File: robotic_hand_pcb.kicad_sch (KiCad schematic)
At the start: 41 parts, among them J1 TC2050-IDC, J2 2171750001, SW1 SPST, SW2 SPST, U1 ld39150dt33-r, U2 STM32F446RET, U3 TXB0104QPWRQ1, Y1 8M, Y2 32k768

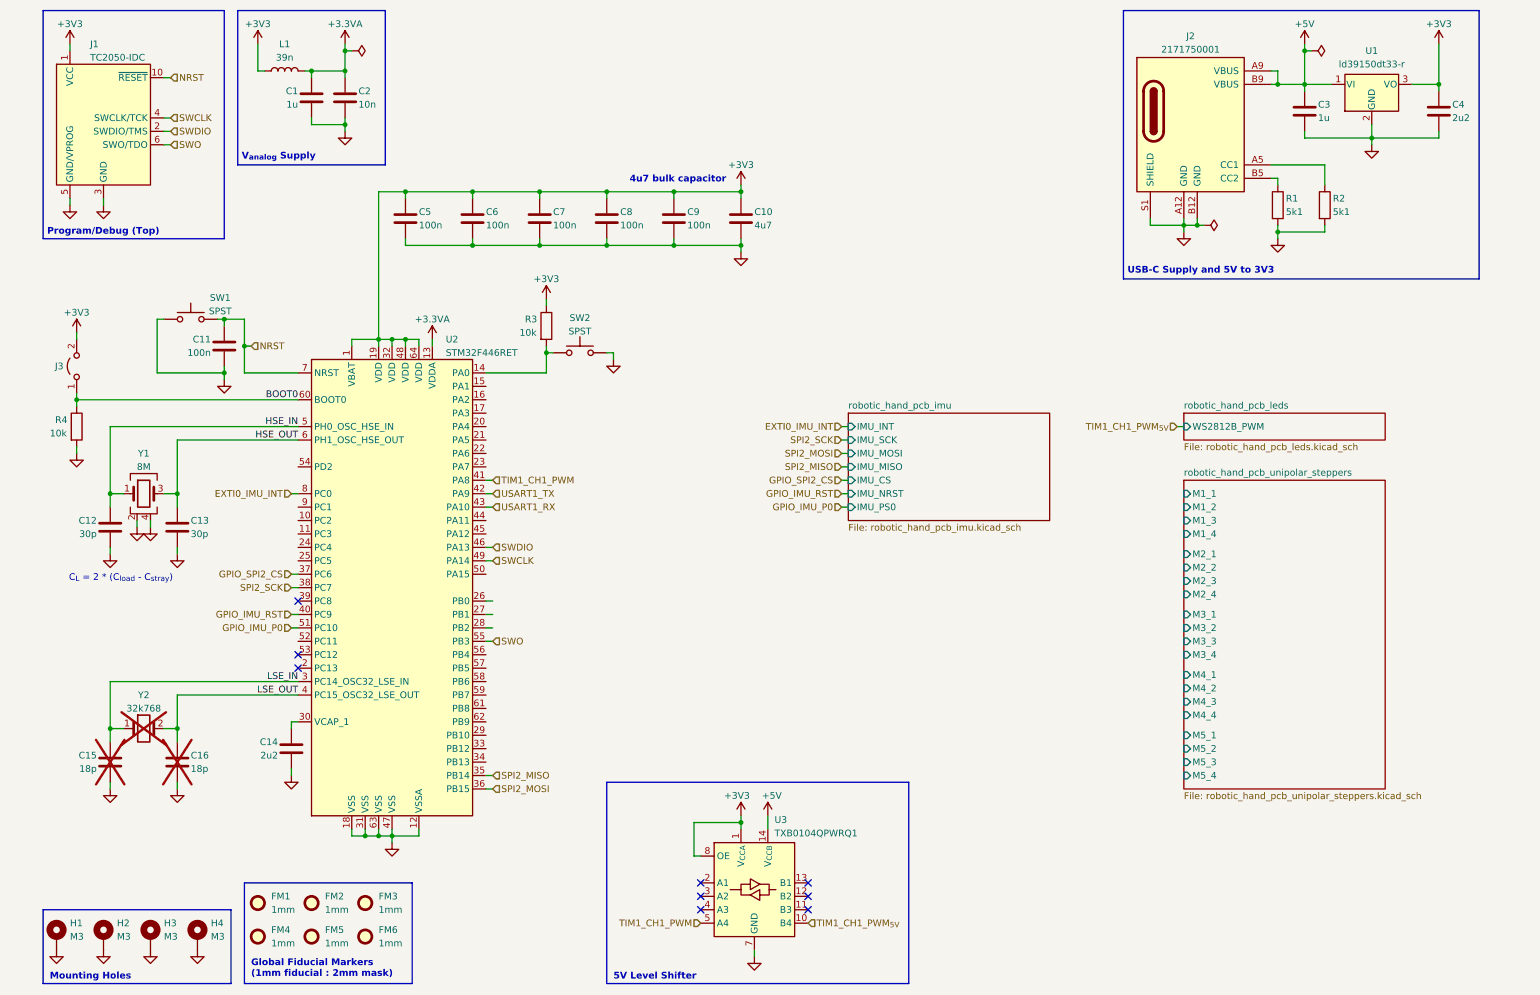
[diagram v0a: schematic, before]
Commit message: Add 5V buck regulator
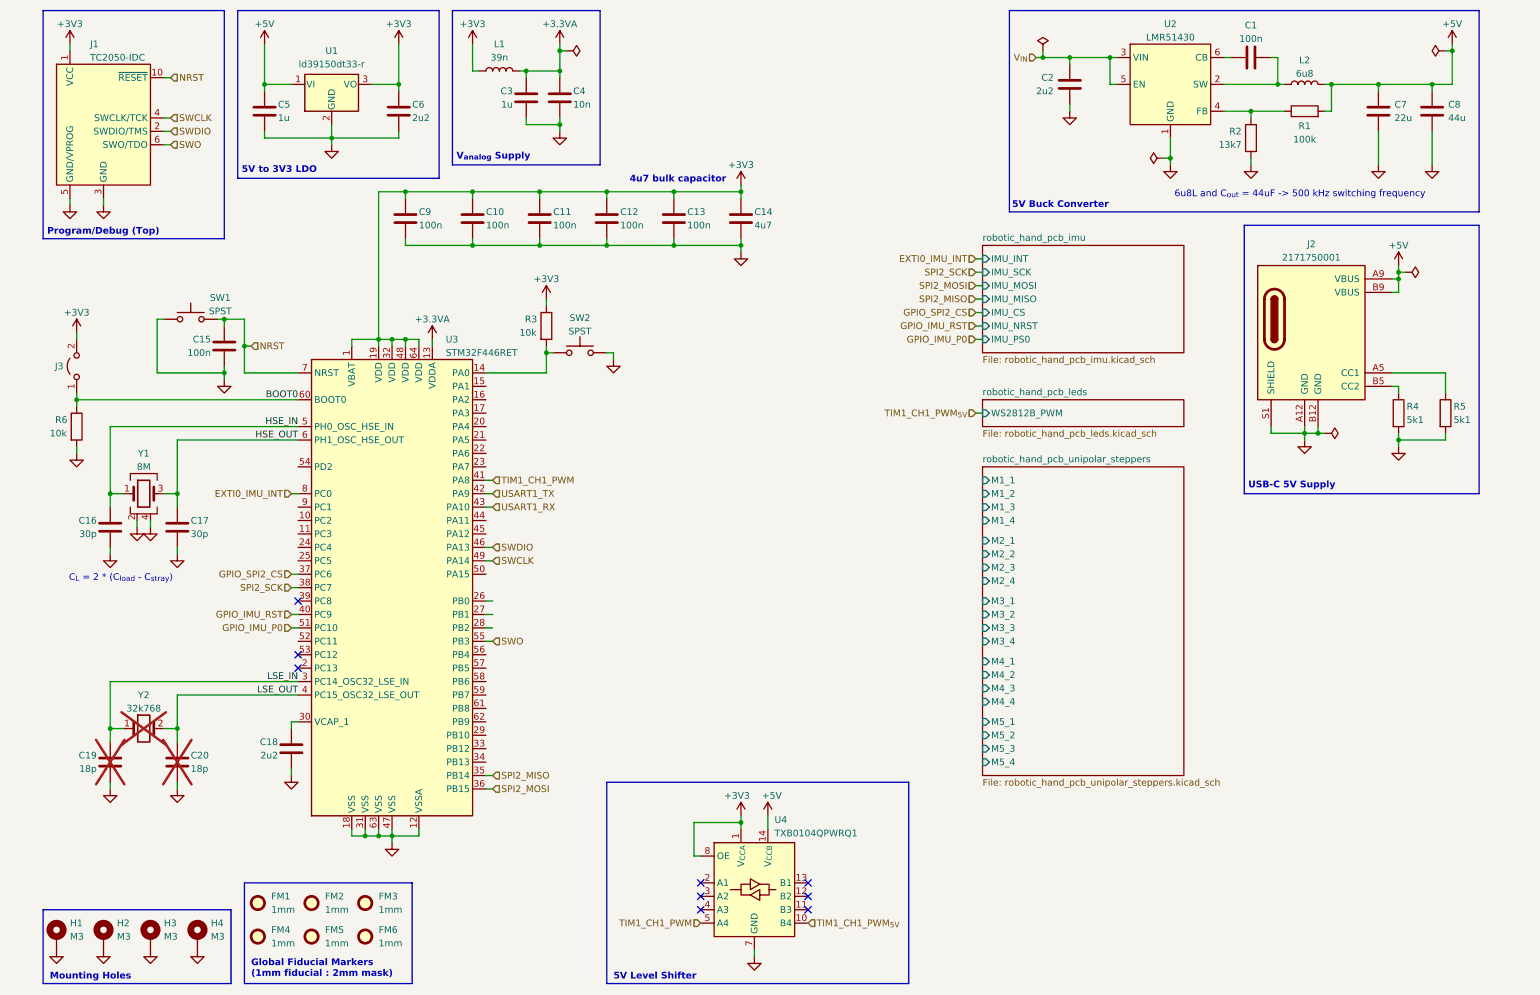
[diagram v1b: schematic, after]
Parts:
- added C1: 100n, symbol Device:C
- added C2: 2u2, symbol Device:C
- added C7: 22u, symbol Device:C
- added C8: 44u, symbol Device:C
- added L2: 6u8, symbol Device:L
- added R1: 100k, symbol Device:R
- added R2: 13k7, symbol Device:R
- added U2: LMR51430, ti_buck:lmr51430, symbol ti_buck:lmr51430
- renumbered C6 to C10, C7 to C11, C8 to C12, C9 to C13, C10 to C14, C11 to C15, C12 to C16, C13 to C17, C14 to C18, C15 to C19, C16 to C20, C1 to C3, C2 to C4, C3 to C5, C4 to C6, C5 to C9, R1 to R4, R2 to R5, R4 to R6, U2 to U3, U3 to U4
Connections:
- net +5V: now also C7.2, C8.2, L2.2, R1.2
- net GND: now also C2.2, C7.1, C8.1, R2.2, U2.1 (GND)
- new net: C1.2, L2.1, U2.2 (SW)
- new net: R1.1, R2.1, U2.4 (FB)
- new net: C1.1, U2.6 (CB)
- new net V_{IN}: C2.1, U2.3 (VIN), U2.5 (EN)
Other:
- note added: "5V Buck Converter"
- note added: "5V to 3V3 LDO"
- note added: "6u8L and C_{out} = 44uF -> 500 kHz switching frequency"
- note added: "USB-C 5V Supply"
- note removed: "USB-C Supply and 5V to 3V3"
- moved on the sheet: C3, C4, C5, C6, J2, L1, R4, R5, U1

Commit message: Pass ERC
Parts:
- removed R3: 10k, Resistor_SMD:R_0603_1608Metric, symbol Device:R
- removed SW2: SPST, Button_Switch_THT:SW_PUSH_6mm, symbol Switch:SW_Push
- added J16: UART, symbol Connector:Conn_01x02_Pin
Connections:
- net USART1_RX: now also J16.2 (Pin_2)
- net USART1_TX: now also J16.1 (Pin_1)
- net ADC_IN12: now reaches U3.10 (PC2)
- net ADC_IN13: now reaches U3.11 (PC3)
- net TIM2_CH1_PWM: now reaches U3.14 (PA0)
- net TIM2_CH2_PWM: now reaches U3.15 (PA1)
- net TIM2_CH3_PWM: now reaches U3.16 (PA2)
- net ADC_IN3: now reaches U3.17 (PA3)
- net ADC_IN4: now reaches U3.20 (PA4)
- net ADC_IN5: now reaches U3.21 (PA5)
- net TIM3_CH1_PWM: now reaches U3.22 (PA6)
- net TIM3_CH2_PWM: now reaches U3.23 (PA7)
- net ADC_IN14: now reaches U3.24 (PC4)
- net ADC_IN15: now reaches U3.25 (PC5)
- net TIM3_CH3_PWM: now reaches U3.26 (PB0)
- net TIM3_CH4_PWM: now reaches U3.27 (PB1)
- net TIM2_CH4_PWM: now reaches U3.28 (PB2)
- net EXTI8_IMU_INT: now reaches U3.39 (PC8)
- net EXTI5_TOF_INT: now reaches U3.57 (PB5)
- net I2C1_SCL: now reaches U3.58 (PB6)
- net I2C1_SDA: now reaches U3.59 (PB7)
- net ADC_IN11: now reaches U3.9 (PC1)
- net EXTI0_IMU_INT renamed ADC_IN10
- no-connect marks 9 -> 19
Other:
- sheet robotic_hand_pcb_unipolar_steppers renamed robotic_hand_pcb_servos
- added sheet robotic_hand_pcb_tof (robotic_hand_pcb_tof.kicad_sch)
- sheet robotic_hand_pcb_leds ports: added ADC_PHOTODIODE; removed none
- sheet robotic_hand_pcb_servos: file robotic_hand_pcb_unipolar_steppers.kicad_sch -> robotic_hand_pcb_servos.kicad_sch
- sheet robotic_hand_pcb_servos ports: added SERVO_1_ISENSE, SERVO_1_PWM, SERVO_2_ISENSE, SERVO_2_PWM, SERVO_3_ISENSE, SERVO_3_PWM, SERVO_4_ISENSE, SERVO_4_PWM, SERVO_5_ISENSE, SERVO_5_PWM, SERVO_6_ISENSE, SERVO_6_PWM, SERVO_7_ISENSE, SERVO_7_PWM, SERVO_8_ISENSE, SERVO_8_PWM; removed M1_1, M1_2, M1_3, M1_4, M2_1, M2_2, M2_3, M2_4, M3_1, M3_2, M3_3, M3_4, M4_1, M4_2, M4_3, M4_4, M5_1, M5_2, M5_3, M5_4
- note added: "UART Breakout"

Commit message: Update for WIP changes
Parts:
- removed C3: 1u, Capacitor_SMD:C_0603_1608Metric, symbol Device:C
- removed C4: 10n, Capacitor_SMD:C_0603_1608Metric, symbol Device:C
- removed L1: 39n, Inductor_SMD:L_0402_1005Metric, symbol Device:L
- removed U1: ld39150dt33-r, common:to-252-2_dpak-2-leg, symbol common:ld39150dt33-r
- added C12: 100n, Capacitor_SMD:C_0603_1608Metric, symbol Device:C
- added U2: ld39150dt33-r, common:to-252-2_dpak-2-leg, symbol common:ld39150dt33-r
- renumbered C12 to C10, C13 to C11, C14 to C13, C15 to C14, C16 to C15, C17 to C16, C18 to C17, C19 to C18, C20 to C19, C7 to C3, C8 to C4, C9 to C7, C10 to C8, C11 to C9, J2 to J1, J1 to J2, J16 to J4, L2 to L1, R4 to R3, R5 to R4, R6 to R5, U2 to U1, U4 to U3, U3 to U4
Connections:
- net +3.3VA is gone; now on net +3V3: U4.13 (VDDA)
- net ADC_IN14 is gone; now on net GPIO_IMU_RST: U4.24 (PC4)
- net ADC_IN15 is gone; now on net GPIO_IMU_P0: U4.25 (PC5)
- net +3V3: now also C12.1, U2.3 (VO)
- net +5V: now also U2.1 (VI)
- net GND: now also C12.2, U2.2 (GND)
- net GPIO_IMU_P0: no longer U4.51 (PC10)
- net GPIO_IMU_RST: no longer U4.40 (PC9)
- net GPIO_ADC_SYNC: now reaches U4.44 (PA11)
- net GPIO_ADC_RST: now reaches U4.45 (PA12)
- net GPIO_SPI3_CS: now reaches U4.50 (PA15)
- net SPI3_MISO: now reaches U4.52 (PC11)
- net SPI3_MOSI: now reaches U4.53 (PC12)
- net EXTI2_ADC_DRDY: now reaches U4.54 (PD2)
- net EXTI4_TOF_INT: now reaches U4.56 (PB4)
- net ADC_IN10: no longer names the net of U4.8 (PC0)
- net ADC_IN11: no longer names the net of U4.9 (PC1)
- net ADC_IN12: no longer names the net of U4.10 (PC2)
- net ADC_IN13: no longer names the net of U4.11 (PC3)
- net ADC_IN3 renamed EXTI3_IMU_INT
- net ADC_IN4 renamed GPIO_SPI1_CS
- net ADC_IN5 renamed SPI1_SCK
- net EXTI5_TOF_INT renamed GPIO_TOF_XSHUT
- net EXTI8_IMU_INT: no longer names the net of U4.39 (PC8)
- net GPIO_SPI2_CS: no longer names the net of U4.37 (PC6)
- net SPI2_MISO: no longer names the net of U4.35 (PB14)
- net SPI2_MOSI: no longer names the net of U4.36 (PB15)
- net SPI2_SCK: no longer names the net of U4.38 (PC7)
- net TIM2_CH1_PWM: no longer names the net of U4.14 (PA0)
- net TIM2_CH2_PWM: no longer names the net of U4.15 (PA1)
- net TIM2_CH3_PWM: no longer names the net of U4.16 (PA2)
- net TIM2_CH4_PWM: no longer names the net of U4.28 (PB2)
- net TIM3_CH1_PWM renamed SPI1_MISO
- net TIM3_CH2_PWM renamed SPI1_MOSI
- net TIM3_CH3_PWM: no longer names the net of U4.26 (PB0)
- net TIM3_CH4_PWM: no longer names the net of U4.27 (PB1)
- new net SPI3_SCK: U4.51 (PC10)
- no-connect marks 19 -> 6
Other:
- sheet robotic_hand_pcb_servos renamed robotic_hand_pcb_unipolar_steppers
- added sheet robotic_hand_pcb_analog (robotic_hand_pcb_analog.kicad_sch)
- sheet robotic_hand_pcb_leds ports: added none; removed ADC_PHOTODIODE
- sheet robotic_hand_pcb_tof ports: added TOF_XSHUT; removed none
- sheet robotic_hand_pcb_unipolar_steppers: file robotic_hand_pcb_servos.kicad_sch -> robotic_hand_pcb_unipolar_steppers.kicad_sch
- sheet robotic_hand_pcb_unipolar_steppers ports: added M1_1, M1_2, M1_3, M1_4, M2_1, M2_2, M2_3, M2_4, M3_1, M3_2, M3_3, M3_4, M4_1, M4_2, M4_3, M4_4, M5_1, M5_2, M5_3, M5_4; removed SERVO_1_ISENSE, SERVO_1_PWM, SERVO_2_ISENSE, SERVO_2_PWM, SERVO_3_ISENSE, SERVO_3_PWM, SERVO_4_ISENSE, SERVO_4_PWM, SERVO_5_ISENSE, SERVO_5_PWM, SERVO_6_ISENSE, SERVO_6_PWM, SERVO_7_ISENSE, SERVO_7_PWM, SERVO_8_ISENSE, SERVO_8_PWM
- note removed: "V_{analog} Supply"
- moved on the sheet: C1, C10, C11, C13, C2, C3, C4, C7, C8, C9, J1, L1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

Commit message: Add WIP schematic changes
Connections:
- net M1_1: now also U4.8 (PC0)
- net M1_2: now also U4.9 (PC1)
- net M1_3: now also U4.10 (PC2)
- net M1_4: now also U4.11 (PC3)
- net M2_1: now also U4.37 (PC6)
- net M2_2: now also U4.38 (PC7)
- net M2_3: now also U4.39 (PC8)
- net M2_4: now also U4.40 (PC9)
- net M3_1: now also U4.14 (PA0)
- net M3_2: now also U4.15 (PA1)
- net M3_3: now also U4.16 (PA2)
- net M3_4: now also U4.26 (PB0)
- net M4_1: now also U4.27 (PB1)
- net M4_2: now also U4.28 (PB2)
- net M4_3: now also U4.61 (PB8)
- net M4_4: now also U4.62 (PB9)
- net M5_1: now also U4.33 (PB12)
- net M5_2: now also U4.34 (PB13)
- net M5_3: now also U4.35 (PB14)
- net M5_4: now also U4.36 (PB15)
- no-connect marks 6 -> 8
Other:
- sheet robotic_hand_pcb_analog ports: added ADC_CS, ADC_DRDY, ADC_MISO, ADC_MOSI, ADC_RST, ADC_SCK, ADC_SYNC; removed none
- sheet robotic_hand_pcb_tof ports: added TOF_SCL, TOF_SDA; removed I2C_SCL, I2C_SDA
- moved on the sheet: J4

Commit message: Assign footprints
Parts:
- C1, C2, C3, C4: footprint (none) -> Capacitor_SMD:C_0603_1608Metric
- J4: footprint (none) -> Connector_PinHeader_2.54mm:PinHeader_1x02_P2.54mm_Vertical
- L1, R1, R2: footprint (none) -> Resistor_SMD:R_0603_1608Metric
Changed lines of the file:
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@@
 			)
 		)
-		(property "Footprint" ""
+		(property "Footprint" "Resistor_SMD:R_0603_1608Metric"
 			(at 105.41 26.67 0)
 			(effects
@@
 			)
 		)
-		(property "Footprint" ""
+		(property "Footprint" "Resistor_SMD:R_0603_1608Metric"
 			(at 97.028 36.83 90)
 			(effects
@@
 			)
 		)
-		(property "Footprint" ""
+		(property "Footprint" "Capacitor_SMD:C_0603_1608Metric"
 			(at 118.4148 27.94 0)
 			(effects
@@
 			)
 		)
-		(property "Footprint" ""
+		(property "Footprint" "Connector_PinHeader_2.54mm:PinHeader_1x02_P2.54mm_Vertical"
 			(at 105.41 187.96 0)
 			(effects
@@
 			)
 		)
-		(property "Footprint" ""
+		(property "Footprint" "Capacitor_SMD:C_0603_1608Metric"
 			(at 128.5748 27.94 0)
 			(effects
@@
 			)
 		)
-		(property "Footprint" ""
+		(property "Footprint" "Capacitor_SMD:C_0603_1608Metric"
 			(at 99.06 20.6248 0)
 			(effects
@@
 			)
 		)
-		(property "Footprint" ""
+		(property "Footprint" "Resistor_SMD:R_0603_1608Metric"
 			(at 105.41 33.528 90)
 			(effects
@@
 			)
 		)
-		(property "Footprint" ""
+		(property "Footprint" "Capacitor_SMD:C_0603_1608Metric"
 			(at 59.9948 30.48 0)
 			(effects

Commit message: Add WIP PCB layout and routing
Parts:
- removed C18, C19: 18p, Capacitor_SMD:C_0402_1005Metric, symbol Device:C
- removed Y2: 32k768, common:ecs_ecx-34r, symbol common:ecs-_327-12_5-34r-c-tr_32k768hz
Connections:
- net EXTI3_IMU_INT is gone; now on net M3_1: U4.17 (PA3)
- net GPIO_SPI1_CS: now also U4.62 (PB9); no longer U4.20 (PA4)
- net M1_1: now also U4.11 (PC3); no longer U4.8 (PC0)
- net M1_2: now also U4.10 (PC2); no longer U4.9 (PC1)
- net M1_3: now also U4.9 (PC1); no longer U4.10 (PC2)
- net M1_4: now also U4.8 (PC0); no longer U4.11 (PC3)
- net M2_1: now also U4.40 (PC9); no longer U4.37 (PC6)
- net M2_2: now also U4.39 (PC8); no longer U4.38 (PC7)
- net M2_3: now also U4.38 (PC7); no longer U4.39 (PC8)
- net M2_4: now also U4.37 (PC6); no longer U4.40 (PC9)
- net M3_1: no longer U4.14 (PA0)
- net M3_2: now also U4.16 (PA2); no longer U4.15 (PA1)
- net M3_3: now also U4.15 (PA1); no longer U4.16 (PA2)
- net M3_4: now also U4.14 (PA0); no longer U4.26 (PB0)
- net M4_1: now also U4.29 (PB10); no longer U4.27 (PB1)
- net M4_3: now also U4.27 (PB1); no longer U4.61 (PB8)
- net M4_4: now also U4.26 (PB0); no longer U4.62 (PB9)
- net M5_1: now also U4.36 (PB15); no longer U4.33 (PB12)
- net M5_2: now also U4.35 (PB14); no longer U4.34 (PB13)
- net M5_3: now also U4.34 (PB13); no longer U4.35 (PB14)
- net M5_4: now also U4.33 (PB12); no longer U4.36 (PB15)
- net LSE_IN: no longer names the net of U4.3 (PC14_OSC32_LSE_IN)
- net LSE_OUT: no longer names the net of U4.4 (PC15_OSC32_LSE_OUT)
- new net EXTI4_IMU_INT: U4.20 (PA4)
- no-connect marks 8 -> 10
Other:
- note added: "LSE_IN"
- note added: "LSE_OUT"

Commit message: Cleanup layout, add WIP routing
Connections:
- net TIM1_CH1_PWM: now also U3.2 (A1); no longer U3.5 (A4)
- net TIM1_CH1_PWM_{5V}: now also U3.13 (B1); no longer U3.10 (B4)
